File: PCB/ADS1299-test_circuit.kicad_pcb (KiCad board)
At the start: 2 copper layers, 115.6 x 90.2 mm, 95 parts, among them J1 CONN_01X07, P1 +5V, P10 CONN_01X03, P11 CONN_01X03, P12 CONN_01X03, P13 CONN_01X03, P14 BiasOut_C, P15 BiasOut_R, P16 BiasIn_C, P17 BiasIn_R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

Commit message: Agrego circuito revisado por Brian y lista de componentes. Falta comprar los capacitores para completar el circuito
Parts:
- moved C10 14.2 mm to (180.3, 99.4)
- moved R3 3.07 mm to (96.3, 98.7)
- moved P23 2.54 mm to (192.9, 123.9), turned to 90 degrees
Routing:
- net GND: track 64.8 -> 152.7 mm, vias 26 -> 23
- net Net-(C12-Pad2): track 222.3 -> 305.4 mm, vias 9 -> 8
- net -2.5: track 116.3 -> 181.9 mm, vias 2 -> 3
- net Net-(C36-Pad2): track 27.2 -> 40.7 mm, vias 1 -> 0
- net +3.3: track 95.9 -> 107.3 mm, vias 1 -> 0
- net Bias: track 91.4 -> 99.5 mm
- net Net-(C36-Pad1): track 20.3 -> 26.1 mm, vias 1 -> 0
- net Net-(C29-Pad2): track 8.90 -> 4.04 mm, vias 1 -> 0
- net Net-(C10-Pad1): track 35.9 -> 40.3 mm
- net Net-(C16-Pad1): track 8.39 -> 4.22 mm, vias 1 -> 0
- net Net-(C23-Pad1): track 8.20 -> 4.07 mm, vias 1 -> 0
- net Net-(C35-Pad2): track 8.14 -> 4.08 mm, vias 1 -> 0
- net Net-(C34-Pad1): track 8.07 -> 4.09 mm, vias 1 -> 0
- net Net-(C28-Pad1): track 8.04 -> 4.17 mm, vias 1 -> 0
- net Net-(C22-Pad2): track 7.67 -> 4.07 mm, vias 1 -> 0
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- removed copper zone on F.Cu, net +2.5
- removed copper zone on F.Cu, net -2.5
- removed copper zone on B.Cu, net GND
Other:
- net class Default: clearance 0.24892 -> 0.2; trace_width 0.6096 -> 0.2; via_dia 0.6 -> 1.2; via_drill 0.4 -> 1
- rule trace_clearance: 0.24892 -> 0.2

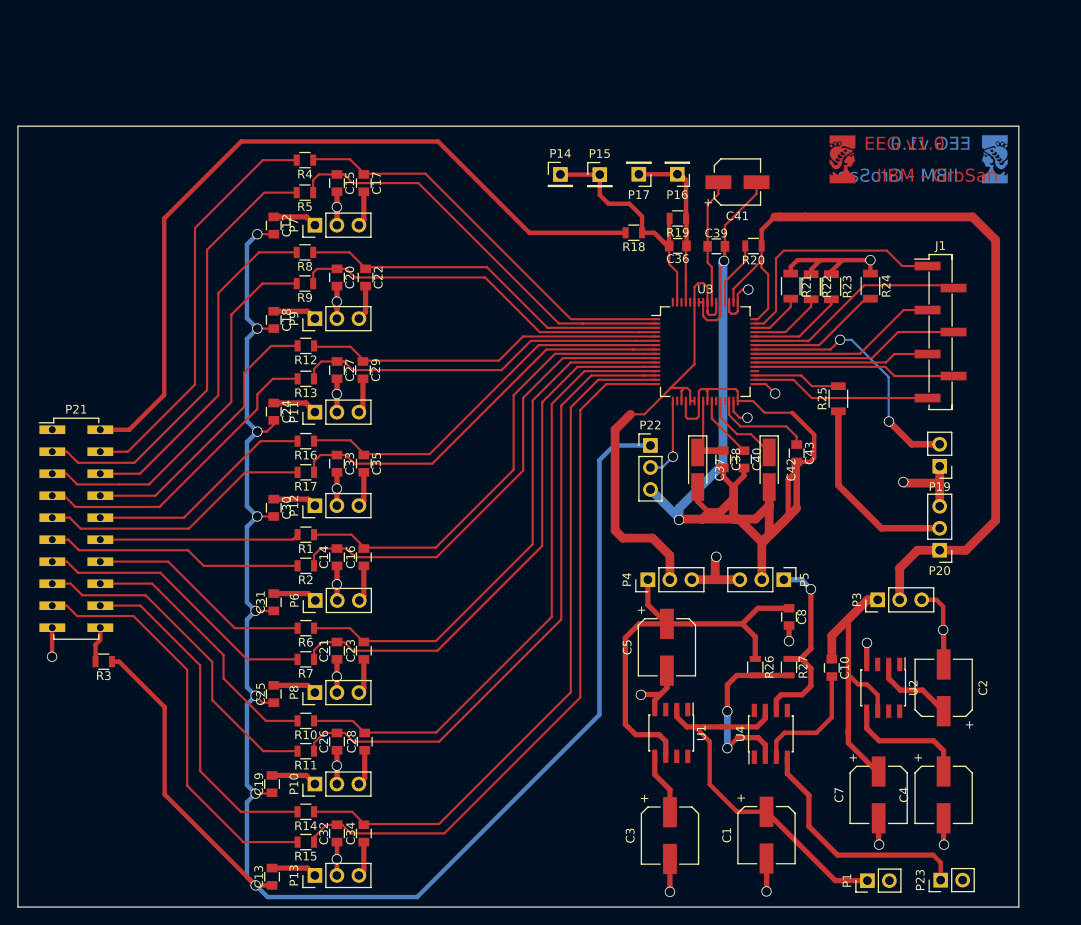
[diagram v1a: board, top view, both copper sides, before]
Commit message: Circuito modificado de acuerdo al tamanio de los capacitores. Tira de pines invertidas
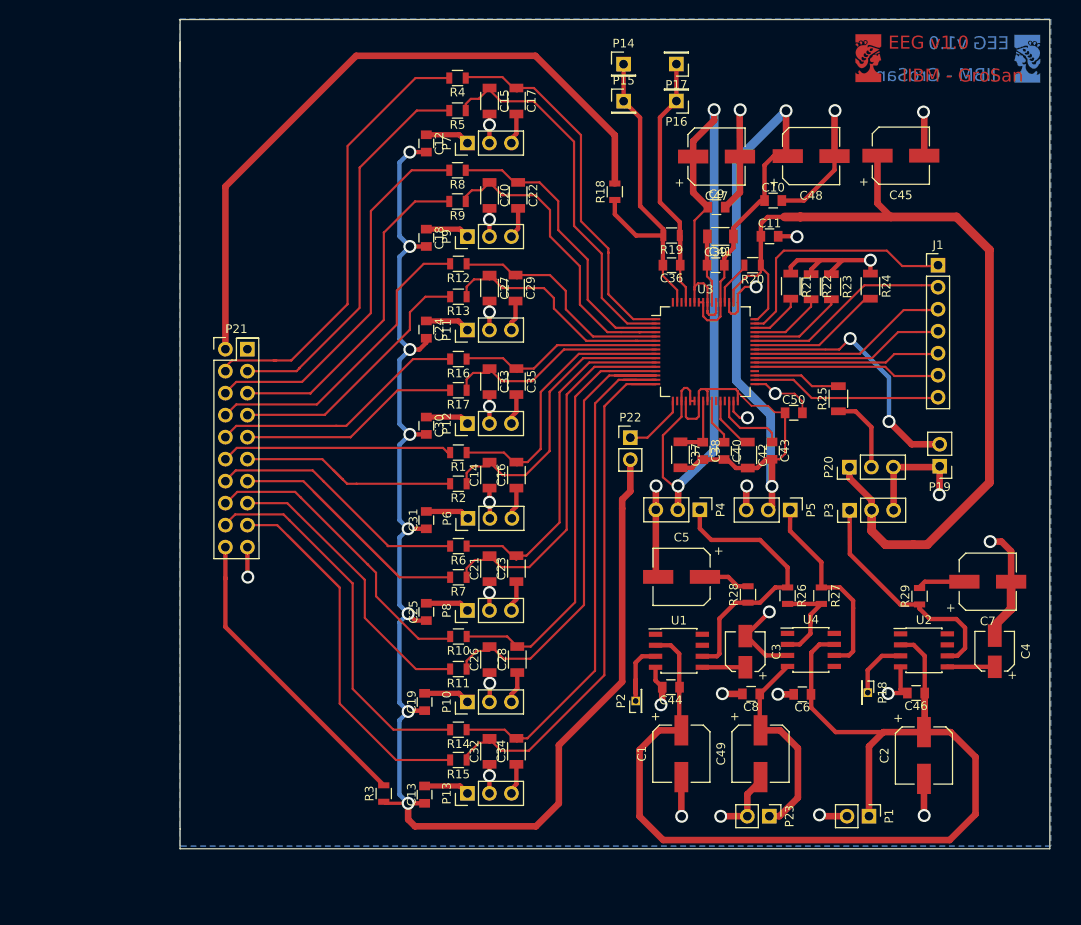
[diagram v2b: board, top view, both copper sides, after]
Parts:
- removed the G*** at (199.1, 40.6)
- removed the G*** at (181.6, 40.6)
- added C11: 0.1u, Capacitors_SMD:C_0805, F.Cu at (173.2, 49.5)
- added C44: 0.1u, Capacitors_SMD:C_0805, F.Cu at (161.8, 101.6)
- added C45: 10u, Capacitors_SMD:CP_Elec_6.3x5.8, F.Cu at (188.3, 40.2)
- added C46: 0.1u, Capacitors_SMD:C_0805, F.Cu at (190.1, 102.3)
- added C47: 10u, Capacitors_SMD:CP_Elec_6.3x5.8, F.Cu at (167.0, 40.3)
- added C48: 10u, Capacitors_SMD:CP_Elec_6.3x5.8, F.Cu at (178.0, 40.3)
- added C49: 10u, Capacitors_SMD:CP_Elec_6.3x5.8, F.Cu at (172.1, 109.3)
- added C50: 0.1u, Capacitors_SMD:C_0805, F.Cu at (175.9, 69.9)
- added C6: 0.1u, Capacitors_SMD:C_0805, F.Cu at (176.9, 102.4)
- added C9: 0.1u, Capacitors_SMD:C_0805, F.Cu at (167.0, 46.2)
- added G***: LOGO, LogoModules:logoFiuba_small_mirrored, F.Cu at (184.6, 29.0)
- added G***: LOGO, LogoModules:logoFiuba_small_mirrored, B.Cu at (202.9, 29.0)
- added P18: Temp5030, Pin_Headers:Pin_Header_Straight_1x01_Pitch1.27mm, F.Cu at (184.5, 102.2)
- added P2: Temp5025, Pin_Headers:Pin_Header_Straight_1x01_Pitch1.27mm, F.Cu at (157.7, 103.2)
- added R28: 1, Resistors_SMD:R_0805, F.Cu at (170.7, 90.9)
- added R29: 1, Resistors_SMD:R_0805, F.Cu at (190.5, 91.1)
- C1, C2: value 1u -> 10u; footprint Capacitors_SMD:CP_Elec_6.3x4.5 -> Capacitors_SMD:CP_Elec_6.3x5.8
- C14, C15, C16, C17, C20, C21, C22, C23, C26, C27, C28, C29, C32, C33, C34, C35: footprint Capacitors_SMD:C_0805 -> Capacitors_SMD:C_1206
- C3, C4: footprint Capacitors_SMD:CP_Elec_6.3x4.5 -> Capacitors_SMD:CP_Elec_4x4.5
- C37, C42: footprint Capacitors_Tantalum_SMD:CP_Tantalum_Case-A_EIA-3216-18_Hand -> Capacitors_SMD:C_1206
- C41: footprint Capacitors_SMD:CP_Elec_5x5.3 -> Capacitors_SMD:C_1206
- C5, C7: footprint Capacitors_SMD:CP_Elec_6.3x4.5 -> Capacitors_SMD:CP_Elec_6.3x5.8
- J1: footprint Pin_Headers:Pin_Header_Straight_1x07_Pitch2.54mm_SMD_Pin1Left -> Pin_Headers:Pin_Header_Straight_1x07_Pitch2.54mm
- P21: footprint Pin_Headers:Pin_Header_Straight_2x10_Pitch2.54mm_SMD -> Pin_Headers_Mirrored:Pin_Header_Straight_2x10_Pitch2.54mm_Mirrored
- P22: footprint Pin_Headers:Pin_Header_Straight_1x03_Pitch2.54mm -> Pin_Headers:Pin_Header_Straight_1x02_Pitch2.54mm
- moved C10 54.4 mm to (173.6, 45.4), turned to 0 degrees
- moved R3 35.7 mm to (128.6, 113.9), turned to 90 degrees
- moved C7 27.7 mm to (198.3, 89.4), turned to 0 degrees
- moved P21 27.0 mm to (110.3, 62.6)
- moved C3 23.0 mm to (170.4, 97.5), turned to 90 degrees
- moved P23 21.1 mm to (173.1, 116.5), turned to 270 degrees
- moved R10 20.1 mm to (137.2, 95.8)
- moved C13 20.0 mm to (133.3, 114.0)
- moved C19 20.0 mm to (133.3, 103.3)
- moved C21 20.0 mm to (140.8, 87.9)
- moved C23 20.0 mm to (143.9, 87.9)
- moved C26 20.0 mm to (140.8, 98.4)
- moved C32 20.0 mm to (140.8, 109.0)
- moved C33 20.0 mm to (140.8, 66.3)
- moved C34 20.0 mm to (143.9, 109.0)
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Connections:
- C10 pad 1: Net-(C10-Pad1) -> -2.5
- C2 pad 1: +4.5 -> +5
- C41 pad 1: Net-(C39-Pad1) -> -2.5
- C41 pad 2: -2.5 -> Net-(C39-Pad1)
- C7 pad 1: Net-(C10-Pad1) -> Net-(C7-Pad1)
- C8 pad 1: Net-(C5-Pad1) -> -5
- P22 pad 1: Net-(C12-Pad2) -> Net-(P22-Pad1)
- P22 pad 2: Net-(P22-Pad2) -> Net-(C12-Pad2)
- P3 pad 1: Net-(C10-Pad1) -> Net-(P3-Pad1)
- P4 pad 1: Net-(C5-Pad1) -> Net-(P4-Pad1)
- R26 pad 1: Net-(C5-Pad1) -> Net-(P4-Pad1)
- U1 pad 6: Net-(C5-Pad1) -> Net-(P4-Pad1)
- U2 pad 2: +4.5 -> +5
- U2 pad 6: Net-(C10-Pad1) -> Net-(P3-Pad1)
- U3 pad 17: Net-(P22-Pad2) -> Net-(P22-Pad1)
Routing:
- net +5: track 43.6 -> 130.2 mm
- net Net-(C12-Pad2): track 305.4 -> 238.5 mm
- net -2.5: track 181.9 -> 125.7 mm, vias 3 -> 2
- net +2.5: track 56.4 -> 104.4 mm, vias 0 -> 2
- net Net-(C5-Pad1): track 48.2 -> 5.42 mm
- net Net-(C10-Pad1): track 40.3 -> 0.00 mm
- net GND: track 152.7 -> 188.1 mm, vias 23 -> 30
- net Net-(P4-Pad1): track 0.00 -> 32.0 mm
- net Ref_elec: track 5.15 -> 35.1 mm
- net Net-(P3-Pad1): track 0.00 -> 26.9 mm
- net +3.3: track 107.3 -> 131.3 mm
- net Net-(C23-Pad2): track 63.1 -> 40.6 mm
- net Net-(C28-Pad2): track 71.7 -> 49.4 mm
- net Net-(C14-Pad2): track 55.9 -> 33.7 mm
- net Net-(C16-Pad2): track 54.4 -> 32.3 mm
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- added copper zone on B.Cu, net GND
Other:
- board size 115.6 x 90.2 mm -> 100.5 x 95.8 mm
- net class Default: clearance 0.2 -> 0.1; via_dia 1.2 -> 1.5
- rule trace_clearance: 0.2 -> 0.1

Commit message: Brian: ajustes del pcb. V1.0
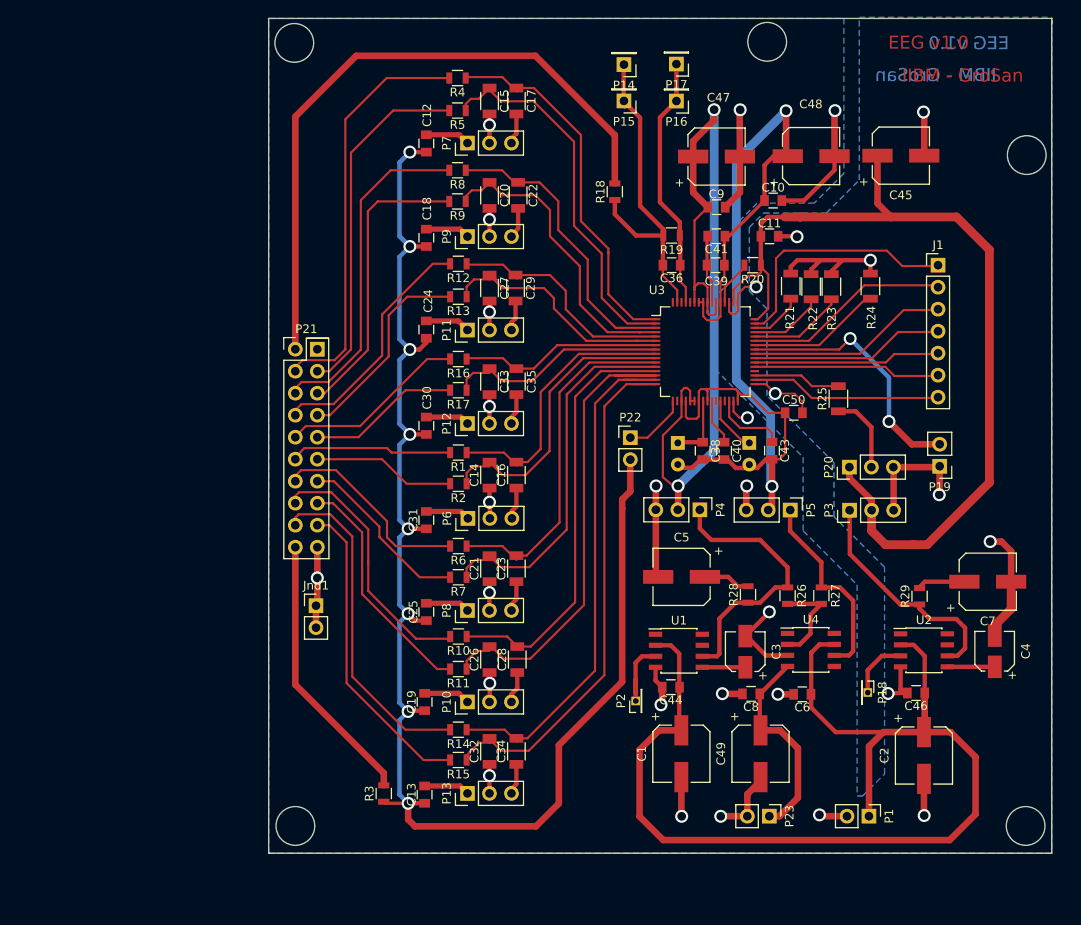
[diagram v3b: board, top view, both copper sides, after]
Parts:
- removed G*** (x2): LOGO, LogoModules:logoFiuba_small_mirrored
- added Jnd1: Gnd, Pin_Headers:Pin_Header_Straight_1x02_Pitch2.54mm, F.Cu at (120.8, 92.2)
- C37, C42: footprint Capacitors_SMD:C_1206 -> Capacitors_THT:CP_Radial_Tantal_D5.0mm_P2.50mm; moved to B.Cu
- C41: footprint Capacitors_SMD:C_1206 -> Capacitors_SMD:C_0805
- moved P21 8.07 mm to (118.4, 62.6)
- moved C42 1.41 mm to (170.8, 73.4)
- moved C37 1.41 mm to (162.6, 73.4)
- moved C41 0.47 mm to (167.0, 49.5)
- moved P14 0.07 mm to (156.3, 29.7), turned to 180 degrees
- turned P15 to 180 degrees
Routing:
- net IN3P: track 42.0 -> 20.6 mm
- net IN1P: track 51.0 -> 36.1 mm
- net IN4P: track 26.1 -> 16.5 mm
- net IN4N: track 27.4 -> 19.0 mm
- net IN5N: track 29.8 -> 21.7 mm
- net IN5P: track 25.7 -> 17.6 mm
- net IN6N: track 35.5 -> 28.2 mm
- net IN3N: track 30.2 -> 23.5 mm
- net IN6P: track 30.3 -> 23.8 mm
- net IN2P: track 33.9 -> 27.4 mm
- net GND: track 188.1 -> 194.0 mm
- net IN1N: track 44.1 -> 38.7 mm
- net IN2N: track 35.2 -> 30.1 mm
- net IN7P: track 38.5 -> 33.8 mm
- net IN7N: track 43.5 -> 38.9 mm
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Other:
- board size 100.5 x 95.8 mm -> 90.4 x 96.4 mm
- net class Default: trace_width 0.2 -> 0.254

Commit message: Agrego pines torneados para GND, logo fiuba y acomodo pistas
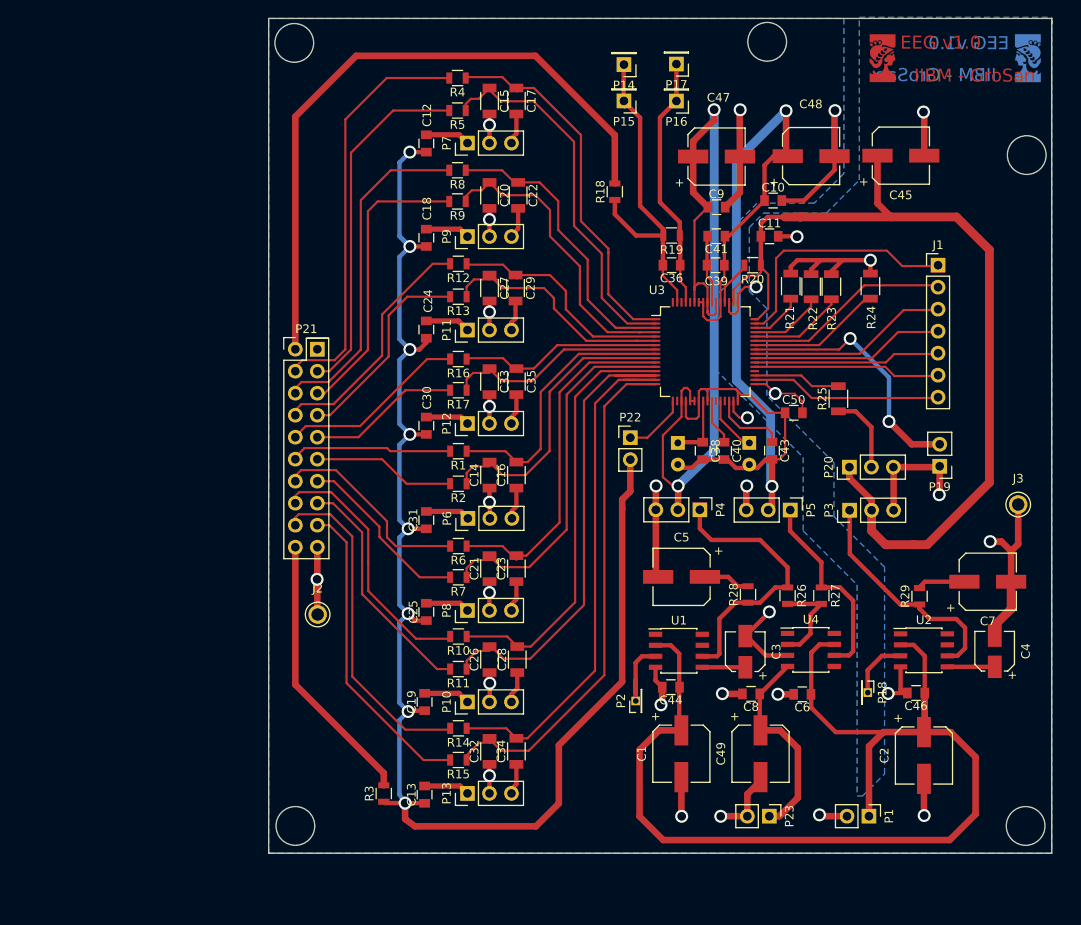
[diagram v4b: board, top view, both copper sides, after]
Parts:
- removed Jnd1: Gnd, Pin_Headers:Pin_Header_Straight_1x02_Pitch2.54mm
- added G***: LOGO, LogoModules:logoFiuba_small_mirrored, F.Cu at (186.2, 29.0)
- added G***: LOGO, LogoModules:logoFiuba_small_mirrored, B.Cu at (202.9, 29.0)
- added J2: CONN_01X01_MALE, PINtorneado:PINtorneado, F.Cu at (121.0, 93.2)
- added J3: CONN_01X01_MALE, PINtorneado:PINtorneado, F.Cu at (201.9, 80.5)
- moved R1 0.16 mm to (137.2, 74.4)
- moved R14 0.16 mm to (137.2, 106.4)
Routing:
- net GND: track 194.0 -> 199.2 mm
- net Net-(C12-Pad2): track 238.5 -> 237.0 mm
